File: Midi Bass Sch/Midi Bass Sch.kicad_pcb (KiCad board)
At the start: 2 copper layers, 171.5 x 114.3 mm, 113 parts, among them J10 A SLAVE ISCP, J11 A Slave OUT, J12 D SLAVE ISCP, J13 D Slave OUT, J14 G SLAVE ISCP, J15 G Slave OUT, J16 Power In, J2 Master ISCP, J3 E SLAVE ISCP, J4 E Slave Out, J6 Pluck ISCP, J7 Pick Unit, J8 Pluck Out, SW2 Master Reset, SW3 E-slave Reset, SW4 A-slave Reset, SW5 D-slave Reset, SW6 G-slave Reset, SW7 Pluck Reset, U1 PIC16F1788, U10 PIC16F1789, U16 LM1117MP-1.8, U2 PIC16F1789, U3 PIC16F1789, U8 PIC16F1789, U9 PIC16F1789

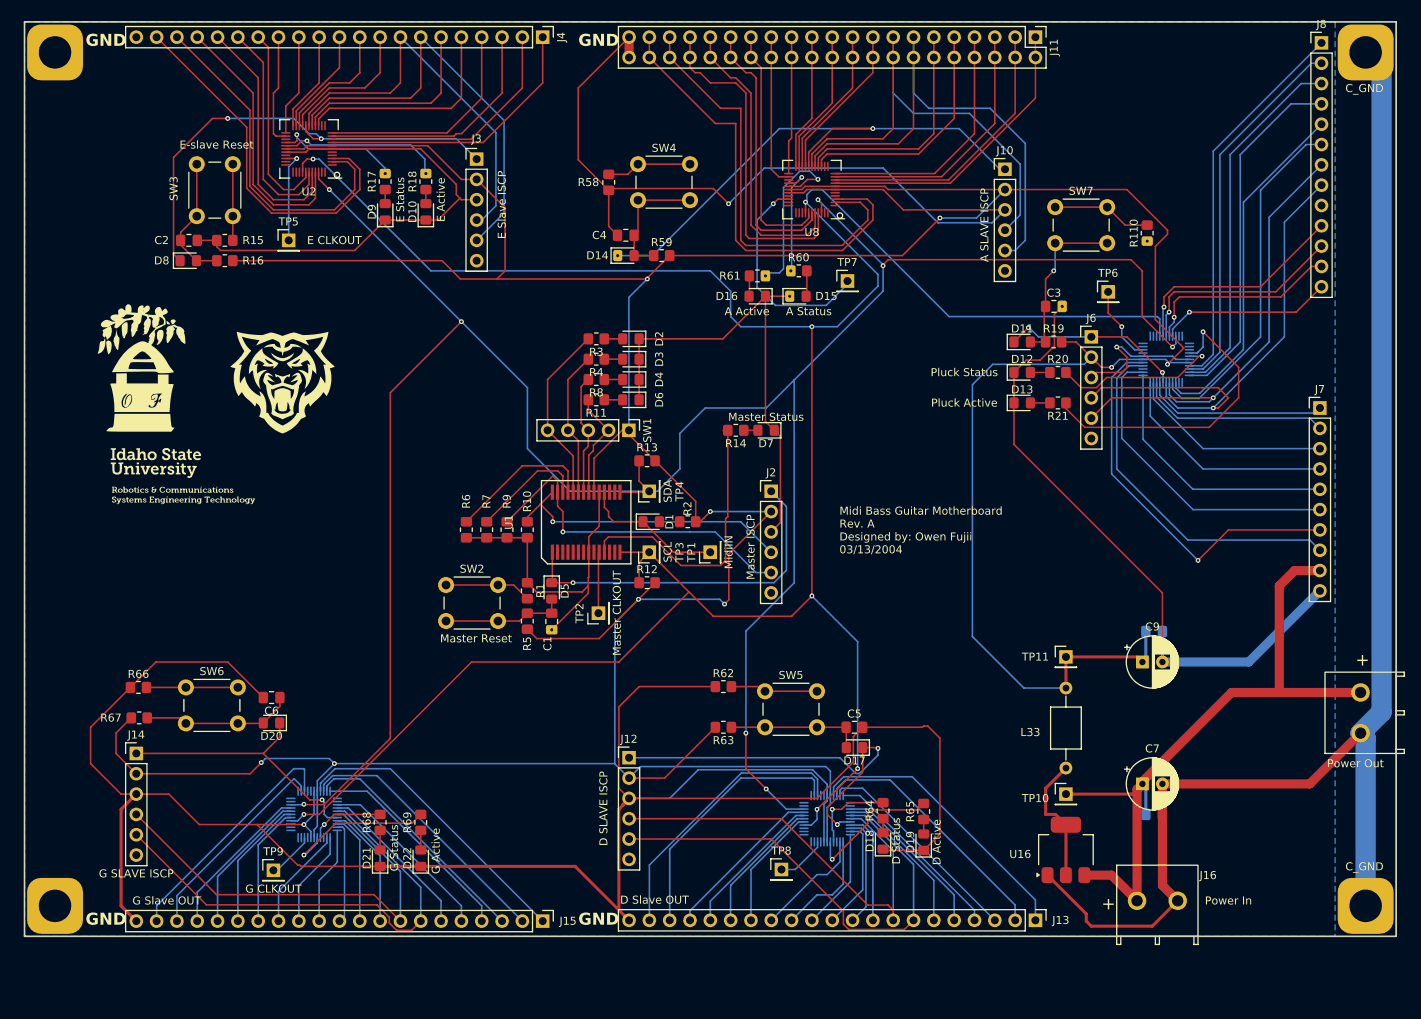
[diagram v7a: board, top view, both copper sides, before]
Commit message: created and generated Rev. B of Motherboard
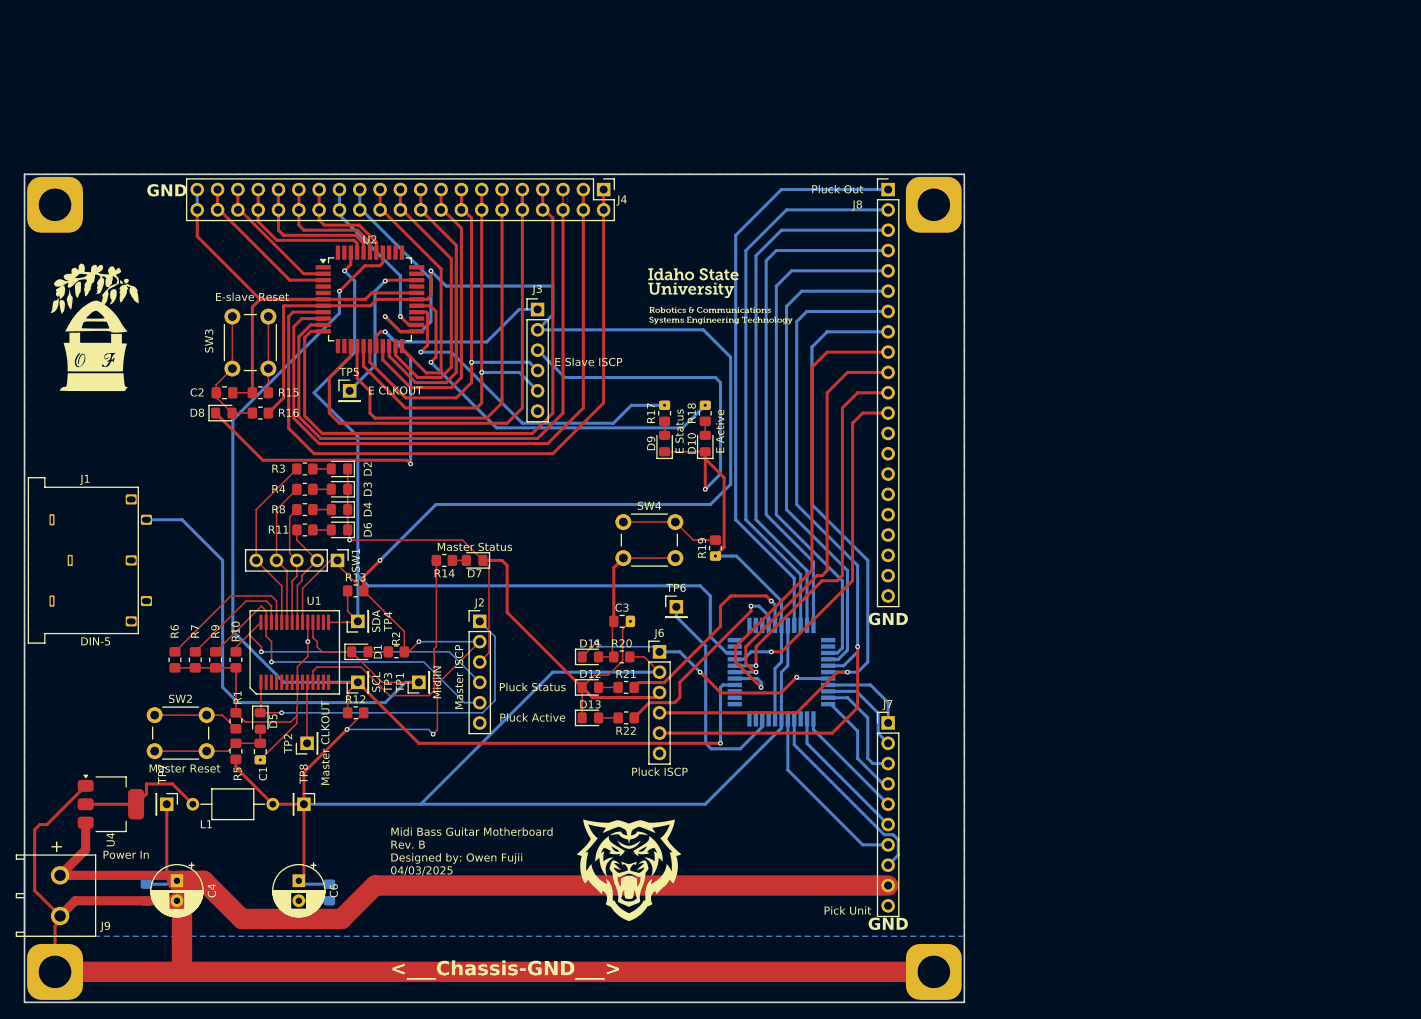
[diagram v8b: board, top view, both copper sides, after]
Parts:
- removed ? (x3): , 
- removed the C4 at (160.9, 135.3)
- removed the C5 at (189.5, 196.8)
- removed the C6 at (116.6, 193.0)
- removed D14, D17, D20: 4148, Diode_SMD:D_0805_2012Metric_Pad1.15x1.40mm_HandSolder
- removed D15: A Status, Diode_SMD:D_0805_2012Metric_Pad1.15x1.40mm_HandSolder
- removed D16: A Active, Diode_SMD:D_0805_2012Metric_Pad1.15x1.40mm_HandSolder
- removed D18: D Status, Diode_SMD:D_0805_2012Metric_Pad1.15x1.40mm_HandSolder
- removed D19: D Active, Diode_SMD:D_0805_2012Metric_Pad1.15x1.40mm_HandSolder
- removed D21: G Status, Diode_SMD:D_0805_2012Metric_Pad1.15x1.40mm_HandSolder
- removed D22: G Active, Diode_SMD:D_0805_2012Metric_Pad1.15x1.40mm_HandSolder
- removed J10: A SLAVE ISCP, Connector_PinHeader_2.54mm:PinHeader_1x06_P2.54mm_Vertical
- removed J11: A Slave OUT, OF Footprints:PinHeader_2x21_P2.54mm_Vertical
- removed J12: D SLAVE ISCP, Connector_PinHeader_2.54mm:PinHeader_1x06_P2.54mm_Vertical
- removed J13: D Slave OUT, Connector_PinHeader_2.54mm:PinHeader_1x21_P2.54mm_Vertical
- removed J14: G SLAVE ISCP, Connector_PinHeader_2.54mm:PinHeader_1x06_P2.54mm_Vertical
- removed J15: G Slave OUT, Connector_PinHeader_2.54mm:PinHeader_1x21_P2.54mm_Vertical
- removed Power Out: Two_Pin_Screw_Terminal, OF Footprints:Two_Pin_Screw_Terminal
- removed R58, R62, R66: 10Ω, Resistor_SMD:R_0805_2012Metric_Pad1.20x1.40mm_HandSolder
- removed R59, R63, R67: 10kΩ, Resistor_SMD:R_0805_2012Metric_Pad1.20x1.40mm_HandSolder
- removed R60, R61, R64, R65, R68, R69: 330Ω, Resistor_SMD:R_0805_2012Metric_Pad1.20x1.40mm_HandSolder
- removed the REF** at (89.5, 219.1)
- removed the SW4 at (162.4, 126.4)
- removed SW5: D-slave Reset, Button_Switch_THT:SW_PUSH_6mm_H5mm
- removed SW6: G-slave Reset, Button_Switch_THT:SW_PUSH_6mm_H5mm
- removed the TP7 at (188.6, 141.0)
- removed the TP8 at (180.3, 214.5)
- removed TP9: G CLKOUT, Connector_PinHeader_2.54mm:PinHeader_1x01_P2.54mm_Vertical
- removed U10, U8, U9: PIC16F1789, OF footprints:TQFN-44_7x7_Pitch0.4mm
- added J1: DIN-5, OF Footprints:Din_5 Connector, F.Cu at (99.1, 175.9)
- added REF**: 6-32 Mount, OF Footprints:6-32 Mount, F.Cu at (199.4, 227.3)
- added REF**: 6-32 Mount, OF Footprints:6-32 Mount, F.Cu at (89.5, 227.3)
- added REF**: 6-32 Mount, OF Footprints:6-32 Mount, F.Cu at (89.5, 131.4)
- added REF**: 6-32 Mount, OF Footprints:6-32 Mount, F.Cu at (199.4, 131.4)
- J4: footprint Connector_PinHeader_2.54mm:PinHeader_1x21_P2.54mm_Vertical -> OF Footprints:PinHeader_2x21_P2.54mm_Vertical
- J8: footprint Connector_PinHeader_2.54mm:PinHeader_1x13_P2.54mm_Vertical -> Connector_PinHeader_2.54mm:PinHeader_1x21_P2.54mm_Vertical
- U2, U3: footprint OF footprints:TQFN-44_7x7_Pitch0.4mm -> OF Footprints:TQFP-44_10x10mm_P0.8mm_Handsolder
- moved J9 137.2 mm to (90.2, 217.8), turned to -90 degrees
- moved C5 126.3 mm to (101.0, 217.4), turned to -90 degrees
- moved C4 121.3 mm to (104.8, 215.9), turned to -90 degrees
- moved U4 119.5 mm to (96.5, 206.4), turned to 0 degrees
- moved TP7 112.4 mm to (103.5, 206.4), turned to -90 degrees
- moved L1 109.2 mm to (106.8, 206.4), turned to 0 degrees
- moved C6 108.9 mm to (120.0, 215.9), turned to -90 degrees
- moved C7 108.1 mm to (123.8, 217.4), turned to -90 degrees
- moved TP8 97.0 mm to (120.7, 206.4), turned to -90 degrees
- moved G*** 74.8 mm to (161.3, 214.6)
- moved G*** 70.8 mm to (169.7, 142.8)
- moved R20 66.8 mm to (160.4, 188.0)
- moved TP6 66.8 mm to (167.2, 181.7)
- moved D11 66.8 mm to (156.5, 188.0)
- moved D12 66.8 mm to (156.5, 191.8)
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- renumbered C7 to C4, C8 to C5, C9 to C6, C10 to C7, J16 to J9, L33 to L1, R110 to R19, R19 to R20, R20 to R21, R21 to R22, SW7 to SW4, TP10 to TP7, TP11 to TP8, U16 to U4
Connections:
- J8 pad 10: /String Strike Slave/E MUTE -> /String Strike Slave/A MUTE
- J8 pad 11: /String Strike Slave/A MUTE -> /String Strike Slave/D MUTE
- J8 pad 12: /String Strike Slave/D MUTE -> /String Strike Slave/G MUTE
- J8 pad 13: /String Strike Slave/G MUTE -> unconnected-(J8-Pad13)
- J8 pad 9: GND -> /String Strike Slave/E MUTE
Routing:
- net GND: track 657.0 -> 274.8 mm
- net I2Cdat: track 307.7 -> 113.4 mm, vias 8 -> 1
- net +5v: track 561.5 -> 370.0 mm, vias 9 -> 5
- net I2Cclk: track 318.0 -> 139.8 mm, vias 7 -> 2
- net MSCLR A: track 68.1 -> 0.00 mm, vias 1 -> 0
- net RB6 A: track 65.2 -> 0.00 mm
- net RB7 A: track 60.0 -> 0.00 mm
- net RB6 G: track 60.0 -> 0.00 mm
- net RB6 D: track 59.1 -> 0.00 mm
- net Net-(U8-RD5/PSMC3E): track 57.5 -> 0.00 mm
- net RB7 G: track 55.6 -> 0.00 mm
- net RB7 D: track 54.7 -> 0.00 mm
- net Net-(D1-K): track 17.8 -> 71.7 mm
- net Net-(U8-RD4/PSM3F): track 53.8 -> 0.00 mm
- net F1: track 35.1 -> 88.7 mm
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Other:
- board size 171.5 x 114.3 mm -> 117.5 x 103.5 mm
- board text added: "<___Chassis-GND___>"
- board text added: "Midi Bass Guitar Motherboard Rev. B Designed by: Owen Fujii 04/03/2025"
- board text removed: "C_GND"
- board text removed: "Midi Bass Guitar Motherboard Rev. A Designed by: Owen Fujii 03/13/2004"
